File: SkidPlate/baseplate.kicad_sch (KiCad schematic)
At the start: 11 parts, among them J11 XT30UPB-M, J12 XT30UPB-M, J13 XT30UPB-M, J14 XT30UPB-M, J3 JST_BM03B-GHS-TBT, J4 JST_BM04B-GHS-TBT, J5 JST_BM04B-GHS-TBT, J6 JST_BM04B-GHS-TBT, J7 JST_BM04B-GHS-TBT

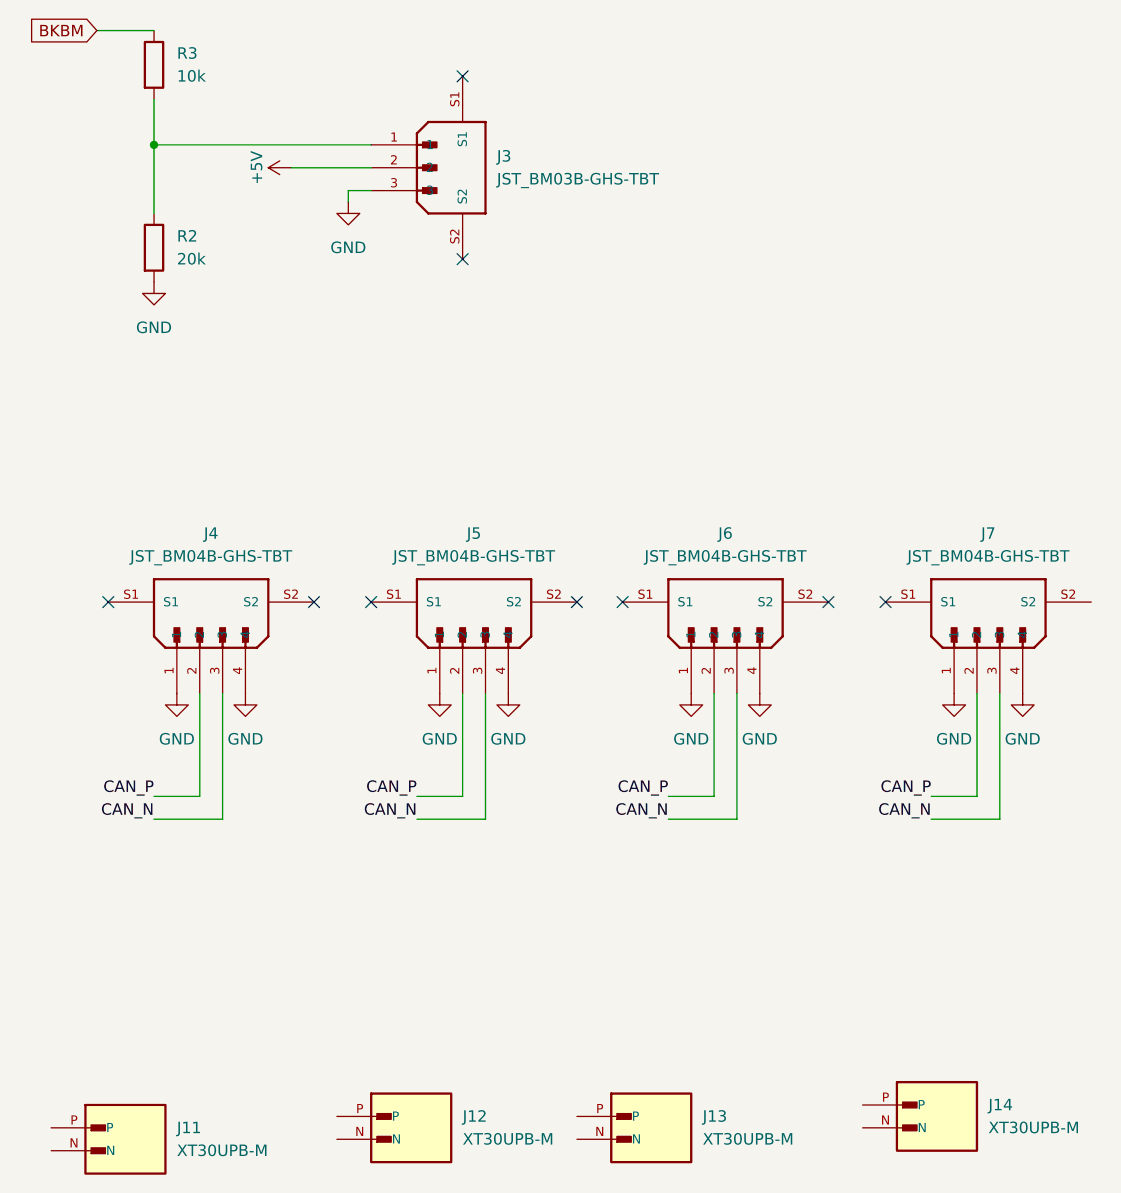
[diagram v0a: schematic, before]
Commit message: skidplate
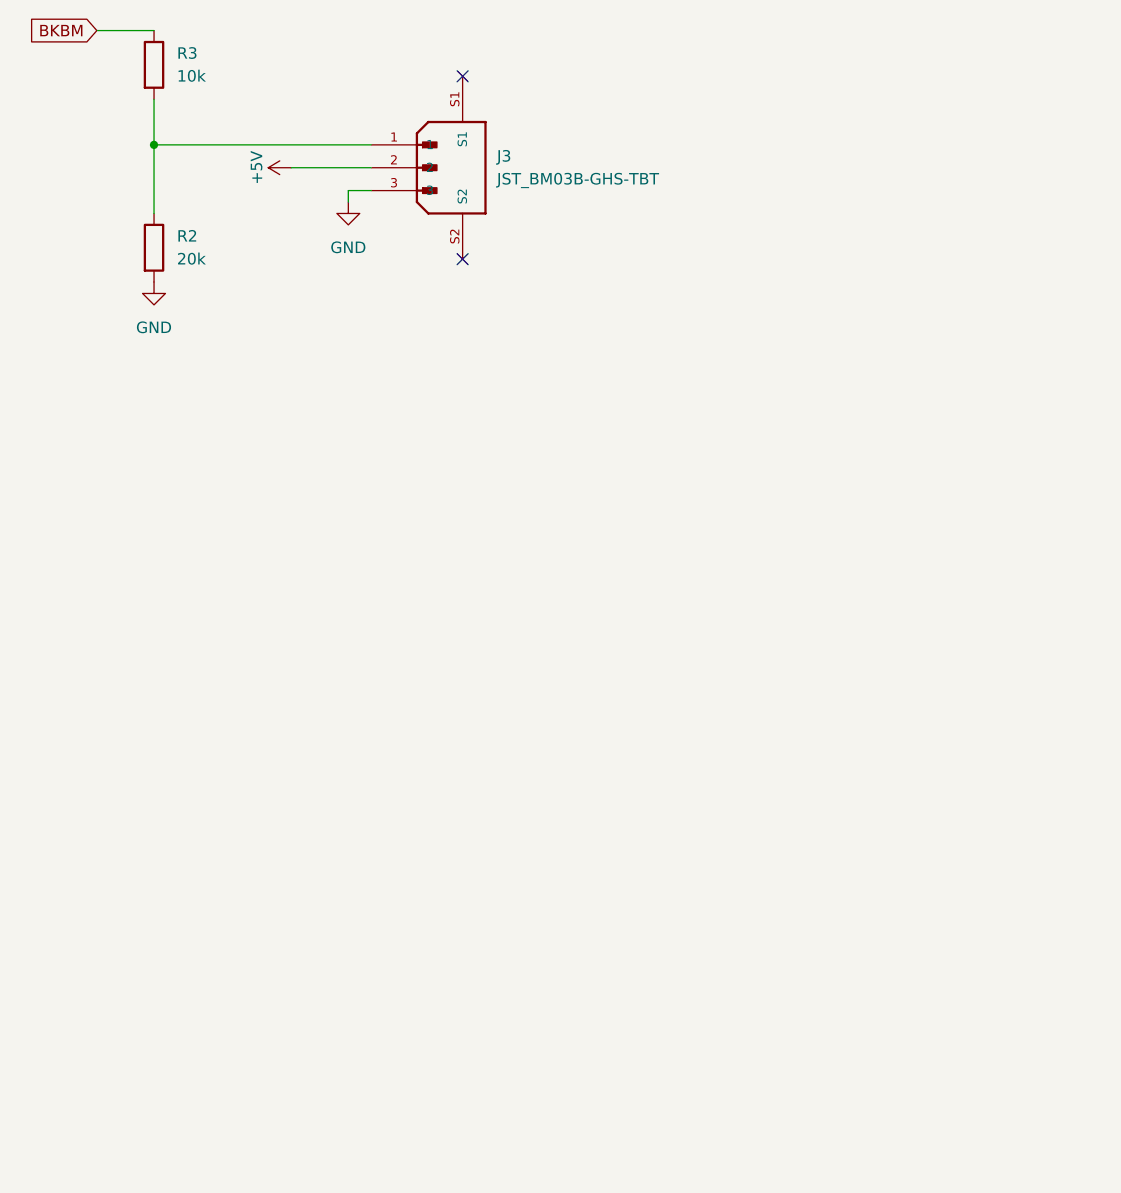
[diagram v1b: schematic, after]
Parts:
- removed J11, J12, J13, J14: XT30UPB-M, bots:AMASS_XT30UPB-M, symbol bots:XT30UPB-M
- removed J4, J5, J6, J7: JST_BM04B-GHS-TBT, bots:JST_BM04B-GHS-TBT, symbol thebots_symlib:JST_BM04B-GHS-TBT
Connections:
- no-connect marks 9 -> 2
